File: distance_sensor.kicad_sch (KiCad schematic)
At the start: 31 parts, among them Q3 IRLML6344T, Q4_5 ST-1KL3A, Q4_6 ST-1KL3A, Q4_7 ST-1KL3A, Q4_8 ST-1KL3A

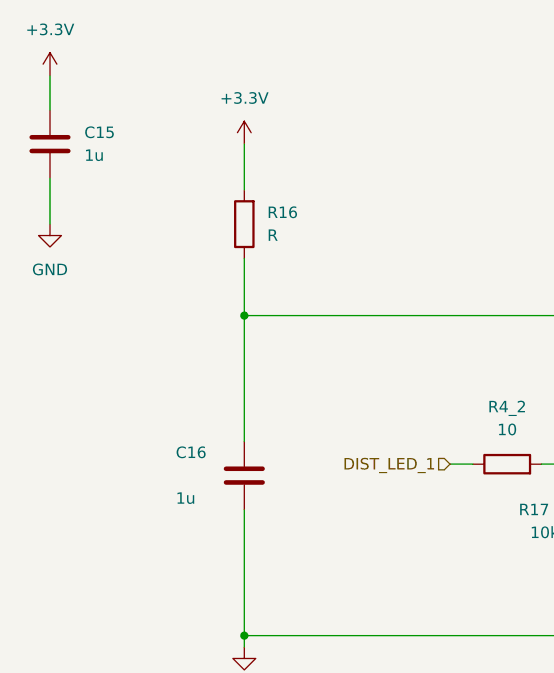
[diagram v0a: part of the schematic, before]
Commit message: コンデンサの表記を統一
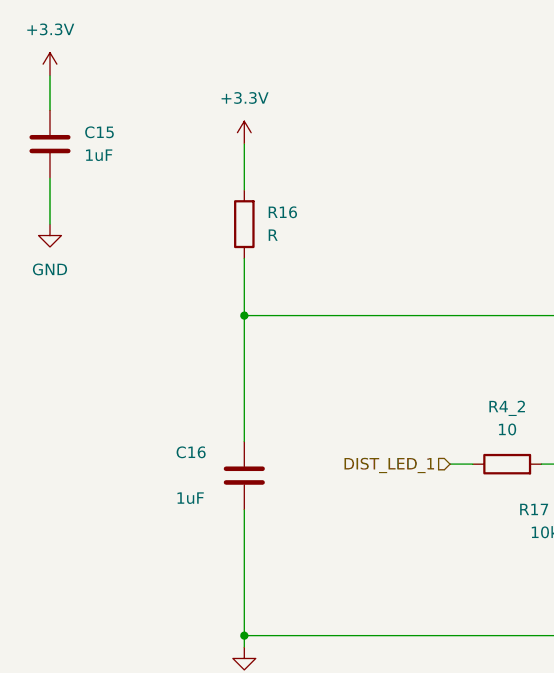
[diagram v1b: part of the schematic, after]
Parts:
- C15, C16: value 1u -> 1uF
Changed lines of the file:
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@@
       (effects (font (size 1.27 1.27)) (justify left))
     )
-    (property "Value" "1u" (at 39.37 74.93 0)
+    (property "Value" "1uF" (at 39.37 74.93 0)
       (effects (font (size 1.27 1.27)) (justify left))
     )
@@
       (effects (font (size 1.27 1.27)) (justify left))
     )
-    (property "Value" "1u" (at 29.21 36.83 0)
-      (effects (font (size 1.27 1.27)) (justify left))
-    )
+    (property "Value" "1uF" (at 29.21 36.83 0)
+      (effects (font (size 1.27 1.27)) (justify left))
+    )

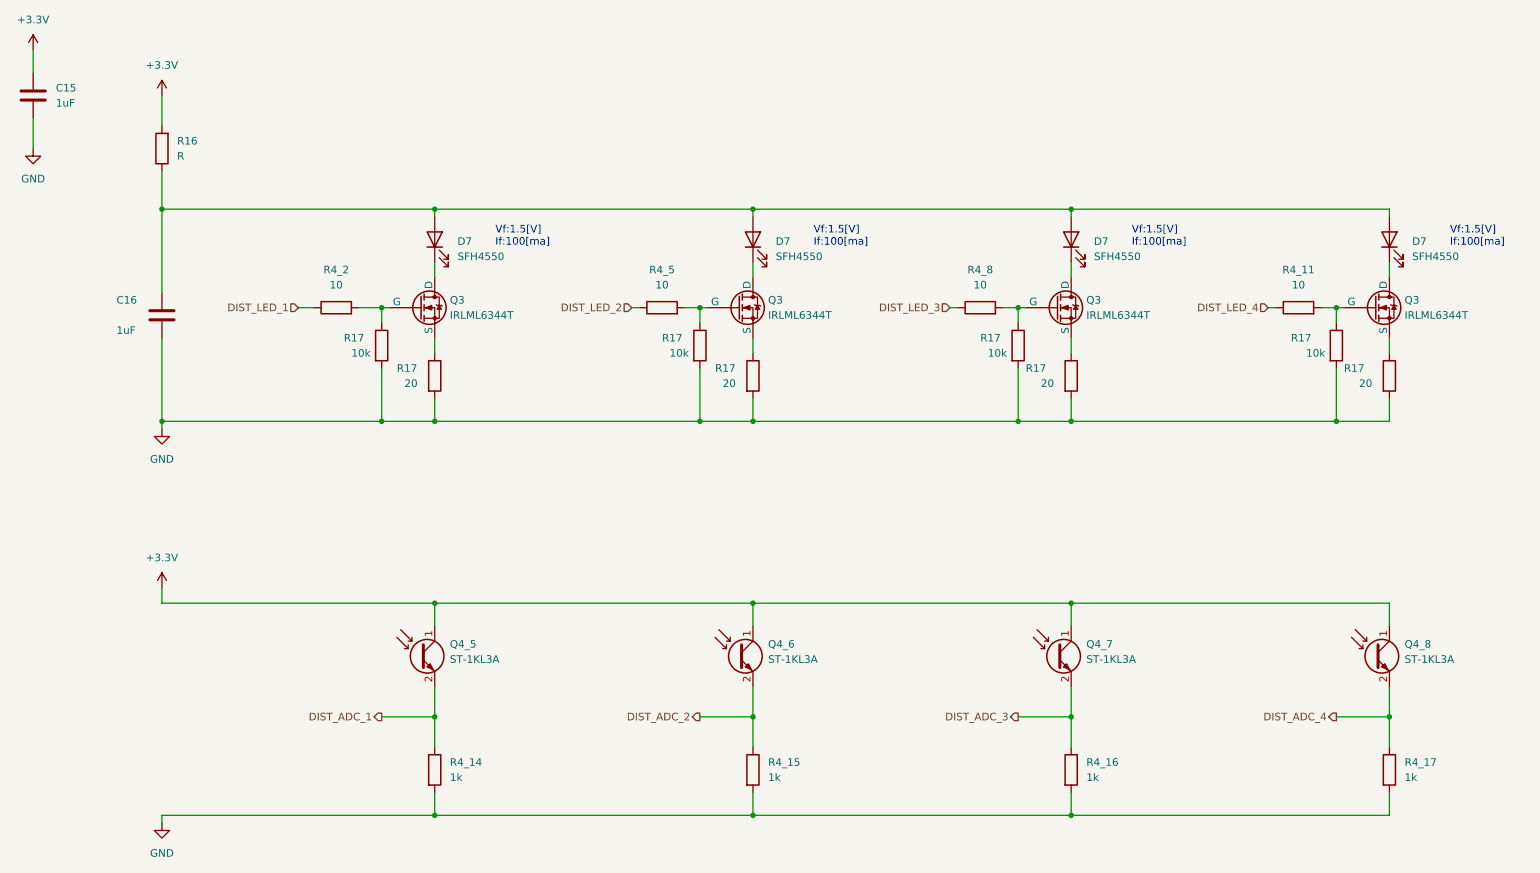
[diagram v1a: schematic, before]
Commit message: 距離センサのLED制限抵抗のミスを修正。アノテーションも振り直した。
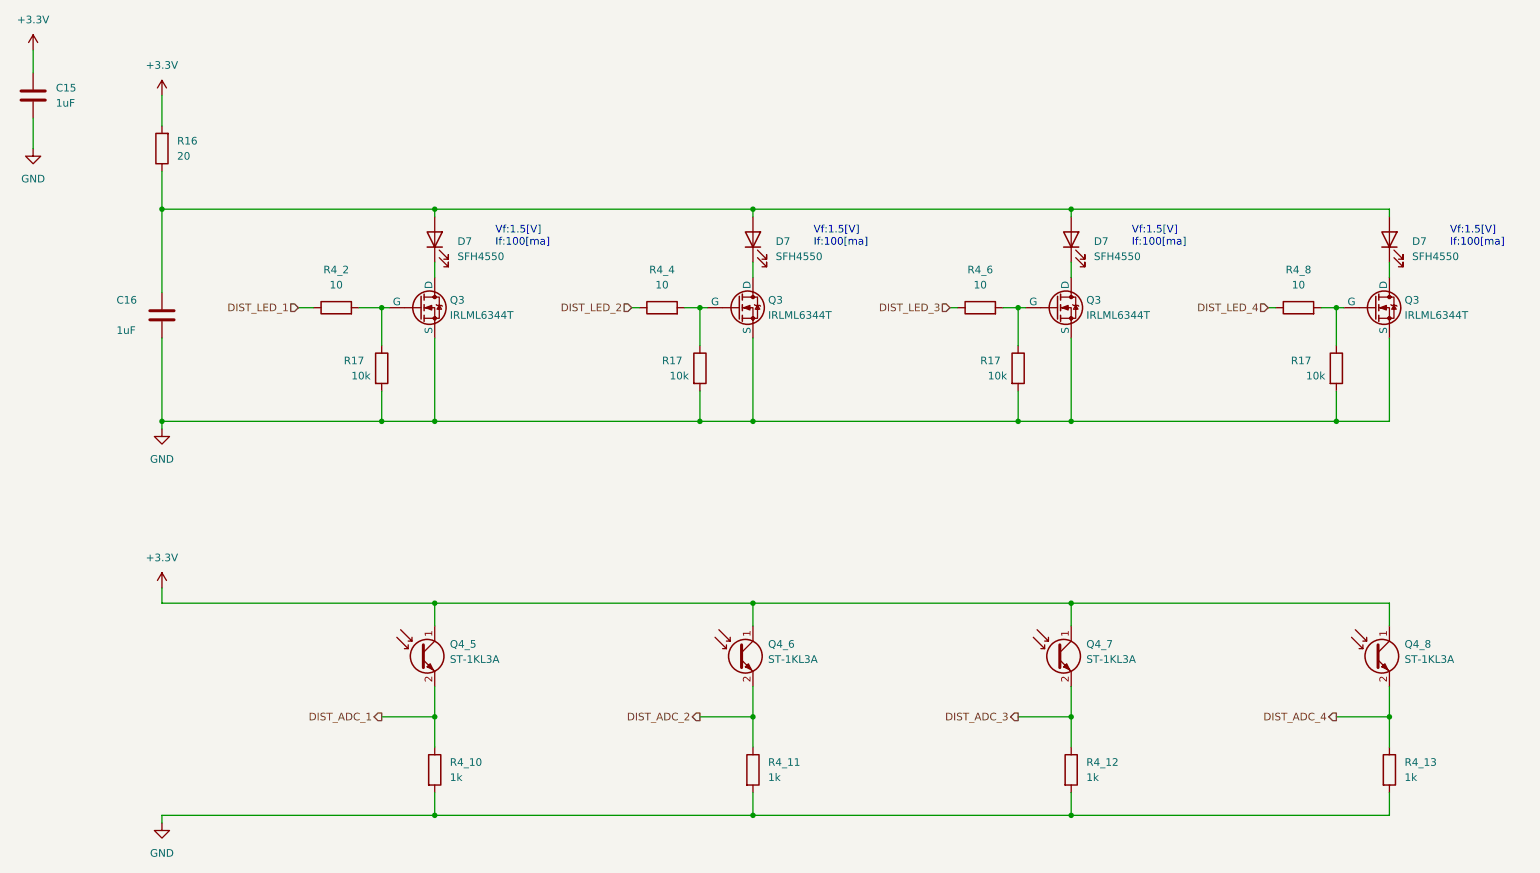
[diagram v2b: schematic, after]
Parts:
- removed R17 (x4): 20, symbol Device:R
- R16: value R -> 20
- renumbered R4_14 to R4_10, R4_15 to R4_11, R4_16 to R4_12, R4_17 to R4_13, R4_5 to R4_4, R4_8 to R4_6, R4_11 to R4_8
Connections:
- net GND: now also Q3.3 (S), Q3.3 (S), Q3.3 (S), Q3.3 (S)
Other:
- moved on the sheet: R17

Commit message: 距離センサに強すぎる電流を抑える制限抵抗追加
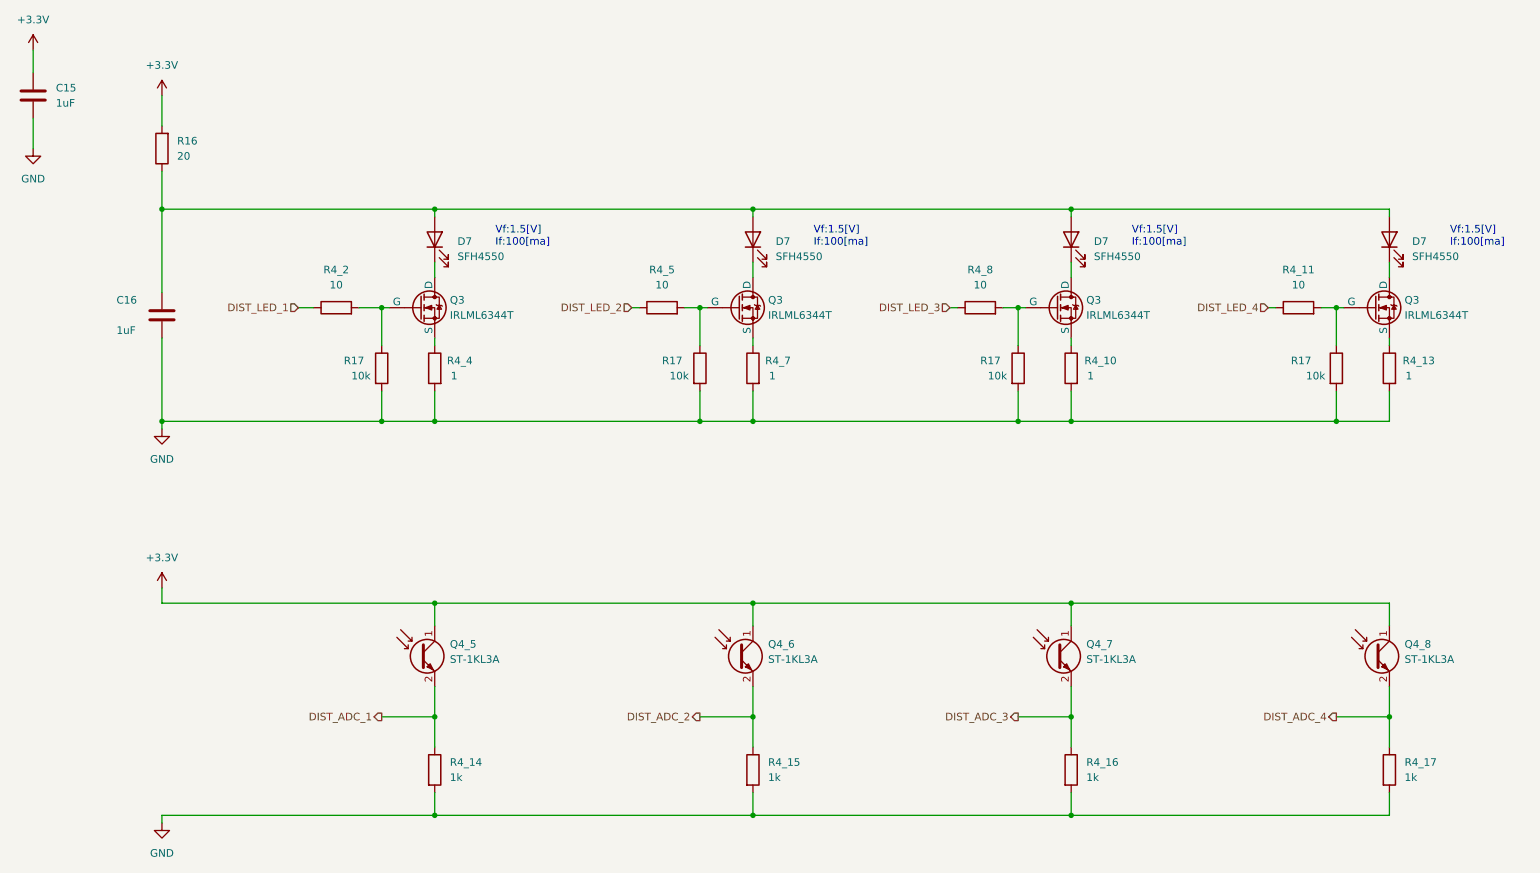
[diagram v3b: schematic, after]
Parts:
- added R4_10, R4_13, R4_4, R4_7: 1, symbol Device:R
- renumbered R4_8 to R4_11, R4_10 to R4_14, R4_11 to R4_15, R4_12 to R4_16, R4_13 to R4_17, R4_4 to R4_5, R4_6 to R4_8
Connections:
- net GND: now also R4_10.2, R4_13.2, R4_4.2, R4_7.2; no longer Q3.3 (S), Q3.3 (S), Q3.3 (S), Q3.3 (S)
- new net: Q3.3 (S), R4_10.1
- new net: Q3.3 (S), R4_7.1
- new net: Q3.3 (S), R4_4.1
- new net: Q3.3 (S), R4_13.1
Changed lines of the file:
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@@
+    (stroke (width 0) (type default))
+  )
+  (wire (pts (xy 252.73 85.09) (xy 252.73 90.17))
+    (stroke (width 0) (type default))
+  )
+  (wire (pts (xy 92.71 85.09) (xy 92.71 90.17))
     (stroke (width 0) (type default))
   )
@@
     (stroke (width 0) (type default))
   )
-  (wire (pts (xy 199.39 76.2) (xy 199.39 90.17))
+  (wire (pts (xy 199.39 76.2) (xy 199.39 77.47))
     (stroke (width 0) (type default))
   )
@@
     (stroke (width 0) (type default))
   )
-  (wire (pts (xy 92.71 76.2) (xy 92.71 90.17))
+  (wire (pts (xy 92.71 76.2) (xy 92.71 77.47))
     (stroke (width 0) (type default))
   )
@@
     (stroke (width 0) (type default))
   )
+  (wire (pts (xy 146.05 85.09) (xy 146.05 90.17))
+    (stroke (width 0) (type default))
+  )
   (wire (pts (xy 199.39 120.65) (xy 146.05 120.65))
     (stroke (width 0) (type default))
@@
     (stroke (width 0) (type default))
   )
-  (wire (pts (xy 146.05 76.2) (xy 146.05 90.17))
+  (wire (pts (xy 199.39 85.09) (xy 199.39 90.17))
+    (stroke (width 0) (type default))
+  )
+  (wire (pts (xy 146.05 76.2) (xy 146.05 77.47))
     (stroke (width 0) (type default))
   )
@@
     (stroke (width 0) (type default))
   )
-  (wire (pts (xy 252.73 76.2) (xy 252.73 90.17))
+  (wire (pts (xy 252.73 76.2) (xy 252.73 77.47))
     (stroke (width 0) (type default))
   )
@@
         )
         (path "/588ca8cd-b11b-4b55-96d9-278aac6cd0cf/dfd8b513-1f63-464b-abba-f89642a821ce"
-          (reference "R4_7") (unit 1)
+          (reference "R4_9") (unit 1)
         )
       )
@@
   (symbol (lib_id "Device:R") (at 146.05 148.59 0) (unit 1)
     (in_bom yes) (on_board yes) (dnp no) (fields_autoplaced)
-    (property "Reference" "R4_11" (at 148.59 147.32 0)
+    (property "Reference" "R4_15" (at 148.59 147.32 0)
       (effects (font (size 1.27 1.27)) (justify left))
     )
@@
       (project "fast_respect"
         (path "/588ca8cd-b11b-4b55-96d9-278aac6cd0cf/dfd8b513-1f63-464b-abba-f89642a821ce"
-          (reference "R4_11") (unit 1)
+          (reference "R4_15") (unit 1)
         )
       )
@@
     )
   )
+  (symbol (lib_id "Device:R") (at 199.39 81.28 0) (mirror y) (unit 1)
+    (in_bom yes) (on_board yes) (dnp no)
+    (property "Reference" "R4_10" (at 207.01 80.01 0)
+      (effects (font (size 1.27 1.27)) (justify left))
+    )
+    (property "Value" "1" (at 203.2 82.55 0)
+      (effects (font (size 1.27 1.27)) (justify left))
+    )
+    (property "Footprint" "" (at 201.168 81.28 90)
+      (effects (font (size 1.27 1.27)) hide)
+    )
+    (property "Datasheet" "~" (at 199.39 81.28 0)
+      (effects (font (size 1.27 1.27)) hide)
+    )
+    (pin "1")
+    (pin "2")
+    (instances
+      (project "fast_respect"
+        (path "/588ca8cd-b11b-4b55-96d9-278aac6cd0cf/dfd8b513-1f63-464b-abba-f89642a821ce"
+          (reference "R4_10") (unit 1)
+        )
+      )
+    )
+  )
   (symbol (lib_id "Device:R") (at 92.71 148.59 0) (unit 1)
     (in_bom yes) (on_board yes) (dnp no) (fields_autoplaced)
-    (property "Reference" "R4_10" (at 95.25 147.32 0)
+    (property "Reference" "R4_14" (at 95.25 147.32 0)
       (effects (font (size 1.27 1.27)) (justify left))
     )
@@
       (project "fast_respect"
         (path "/588ca8cd-b11b-4b55-96d9-278aac6cd0cf/dfd8b513-1f63-464b-abba-f89642a821ce"
-          (reference "R4_10") (unit 1)
+          (reference "R4_14") (unit 1)
         )
       )
@@
   (symbol (lib_id "Device:R") (at 237.49 71.12 90) (unit 1)
     (in_bom yes) (on_board yes) (dnp no) (fields_autoplaced)
-    (property "Reference" "R4_8" (at 237.49 64.77 90)
+    (property "Reference" "R4_11" (at 237.49 64.77 90)
       (effects (font (size 1.27 1.27)))
     )
@@
       (project "fast_respect"
         (path "/588ca8cd-b11b-4b55-96d9-278aac6cd0cf/dfd8b513-1f63-464b-abba-f89642a821ce"
-          (reference "R4_8") (unit 1)
+          (reference "R4_11") (unit 1)
         )
       )
@@
   (symbol (lib_id "Device:R") (at 130.81 71.12 90) (unit 1)
     (in_bom yes) (on_board yes) (dnp no) (fields_autoplaced)
-    (property "Reference" "R4_4" (at 130.81 64.77 90)
+    (property "Reference" "R4_5" (at 130.81 64.77 90)
       (effects (font (size 1.27 1.27)))
     )
@@
     )
     (property "Datasheet" "~" (at 130.81 71.12 0)
+      (effects (font (size 1.27 1.27)) hide)
+    )
+    (pin "1")
+    (pin "2")
+    (instances
+      (project "fast_respect"
+        (path "/588ca8cd-b11b-4b55-96d9-278aac6cd0cf/dfd8b513-1f63-464b-abba-f89642a821ce"
+          (reference "R4_5") (unit 1)
+        )
+      )
+    )
+  )
+  (symbol (lib_id "Device:R") (at 92.71 81.28 0) (mirror y) (unit 1)
+    (in_bom yes) (on_board yes) (dnp no)
+    (property "Reference" "R4_4" (at 99.06 80.01 0)
+      (effects (font (size 1.27 1.27)) (justify left))
+    )
+    (property "Value" "1" (at 96.52 82.55 0)
+      (effects (font (size 1.27 1.27)) (justify left))
+    )
+    (property "Footprint" "" (at 94.488 81.28 90)
+      (effects (font (size 1.27 1.27)) hide)
+    )
+    (property "Datasheet" "~" (at 92.71 81.28 0)
       (effects (font (size 1.27 1.27)) hide)
     )
@@
         )
         (path "/588ca8cd-b11b-4b55-96d9-278aac6cd0cf/dfd8b513-1f63-464b-abba-f89642a821ce"
-          (reference "R4_9") (unit 1)
+          (reference "R4_12") (unit 1)
+        )
+      )
+    )
+  )
+  (symbol (lib_id "Device:R") (at 252.73 81.28 0) (mirror y) (unit 1)
+    (in_bom yes) (on_board yes) (dnp no)
+    (property "Reference" "R4_13" (at 260.35 80.01 0)
+      (effects (font (size 1.27 1.27)) (justify left))
+    )
+    (property "Value" "1" (at 256.54 82.55 0)
+      (effects (font (size 1.27 1.27)) (justify left))
+    )
+    (property "Footprint" "" (at 254.508 81.28 90)
+      (effects (font (size 1.27 1.27)) hide)
+    )
+    (property "Datasheet" "~" (at 252.73 81.28 0)
+      (effects (font (size 1.27 1.27)) hide)
+    )
+    (pin "1")
+    (pin "2")
+    (instances
+      (project "fast_respect"
+        (path "/588ca8cd-b11b-4b55-96d9-278aac6cd0cf/dfd8b513-1f63-464b-abba-f89642a821ce"
+          (reference "R4_13") (unit 1)
         )
       )
@@
     )
   )
+  (symbol (lib_id "Device:R") (at 146.05 81.28 0) (mirror y) (unit 1)
+    (in_bom yes) (on_board yes) (dnp no)
+    (property "Reference" "R4_7" (at 152.4 80.01 0)
+      (effects (font (size 1.27 1.27)) (justify left))
+    )
+    (property "Value" "1" (at 149.86 82.55 0)
+      (effects (font (size 1.27 1.27)) (justify left))
+    )
+    (property "Footprint" "" (at 147.828 81.28 90)
+      (effects (font (size 1.27 1.27)) hide)
+    )
+    (property "Datasheet" "~" (at 146.05 81.28 0)
+      (effects (font (size 1.27 1.27)) hide)
+    )
+    (pin "1")
+    (pin "2")
+    (instances
+      (project "fast_respect"
+        (path "/588ca8cd-b11b-4b55-96d9-278aac6cd0cf/dfd8b513-1f63-464b-abba-f89642a821ce"
+          (reference "R4_7") (unit 1)
+        )
+      )
+    )
+  )
   (symbol (lib_id "Device:R") (at 252.73 148.59 0) (unit 1)
     (in_bom yes) (on_board yes) (dnp no) (fields_autoplaced)
-    (property "Reference" "R4_13" (at 255.27 147.32 0)
+    (property "Reference" "R4_17" (at 255.27 147.32 0)
       (effects (font (size 1.27 1.27)) (justify left))
     )
@@
       (project "fast_respect"
         (path "/588ca8cd-b11b-4b55-96d9-278aac6cd0cf/dfd8b513-1f63-464b-abba-f89642a821ce"
-          (reference "R4_13") (unit 1)
+          (reference "R4_17") (unit 1)
         )
       )
@@
         )
         (path "/588ca8cd-b11b-4b55-96d9-278aac6cd0cf/dfd8b513-1f63-464b-abba-f89642a821ce"
-          (reference "R4_5") (unit 1)
+          (reference "R4_6") (unit 1)
         )
       )
@@
   (symbol (lib_id "Device:R") (at 199.39 148.59 0) (unit 1)
     (in_bom yes) (on_board yes) (dnp no) (fields_autoplaced)
-    (property "Reference" "R4_12" (at 201.93 147.32 0)
+    (property "Reference" "R4_16" (at 201.93 147.32 0)
       (effects (font (size 1.27 1.27)) (justify left))
     )
@@
       (project "fast_respect"
         (path "/588ca8cd-b11b-4b55-96d9-278aac6cd0cf/dfd8b513-1f63-464b-abba-f89642a821ce"
-          (reference "R4_12") (unit 1)
+          (reference "R4_16") (unit 1)
         )
       )
@@
   (symbol (lib_id "Device:R") (at 184.15 71.12 90) (unit 1)
     (in_bom yes) (on_board yes) (dnp no) (fields_autoplaced)
-    (property "Reference" "R4_6" (at 184.15 64.77 90)
+    (property "Reference" "R4_8" (at 184.15 64.77 90)
       (effects (font (size 1.27 1.27)))
     )
@@
       (project "fast_respect"
         (path "/588ca8cd-b11b-4b55-96d9-278aac6cd0cf/dfd8b513-1f63-464b-abba-f89642a821ce"
-          (reference "R4_6") (unit 1)
-        )
-      )
+          (reference "R4_8") (unit 1)
+        )
+      )
